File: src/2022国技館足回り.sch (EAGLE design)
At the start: 12 parts

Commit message: 国技館足回り回路の追加
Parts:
- removed MAT_LED: 02-JST, con-jst-xh:02-JST
- added C1: 100nF, rcl:C-EU025-024X044
- added LED1, LED2, LED3, LED4, LED5, LED6: (no value), led:LED5MM
- added POW: 02-JST, con-jst-xh:02-JST
- added R1, R2, R3, R4, R5, R6: 100, rcl:R-EU_0204/7
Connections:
- new net BUSY: JP1.38, JP8.1
- new net LED1: JP2.22, R2.1
- new net LED2: JP2.24, R3.1
- new net LED3: JP2.26, R4.1
- new net LED4: JP2.28, R5.1
- new net LED5: JP2.30, R6.1
- new net N$1: LED3.A, R3.2
- new net N$2: LED2.A, R2.2
- new net N$3: LED1.A, R1.2
- new net N$5: LED6.A, R6.2
- new net N$6: LED5.A, R5.2
- new net N$7: LED4.A, R4.2
- new net RESET: JP1.32, JP8.8
- new net SLEEP: JP1.30, JP9.2
- new net STATUS: JP1.34, JP8.6
- new net VIN: C1.1, JP1.24, POW.2, R1.1
- new net XMIT: JP1.36, JP8.2
- net 3V3: now also JP1.16, JP8.7
- net 5V: now also JP1.18
- net ENC1_A: now also JP1.15
- net ENC1_B: now also JP1.13
- net ENC2_A: now also JP1.27
- net ENC2_B: now also JP1.25
- net ENC3_A: now also JP1.31
- net ENC3_B: now also JP1.29
- net ENC4_A: now also JP1.37
- net ENC4_B: now also JP1.35
- net GND: now also C1.2, JP1.20, JP9.8, LED1.C, LED2.C, LED3.C, LED4.C, LED5.C, LED6.C, POW.1
- net RX1: now also JP1.21, JP8.4; no longer MAT_LED.1
- net SCL: now also JP2.3
- net SDA: now also JP2.5
- net TX1: now also JP1.17, JP9.3; no longer MAT_LED.2
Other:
- note added: "IM920sL"
- note added: "LED"
- note added: "NUCLEO-F411RE"
- note added: "POW"
- moved on the sheet: JP1, JP2, JP8, JP9, SUSPENSION

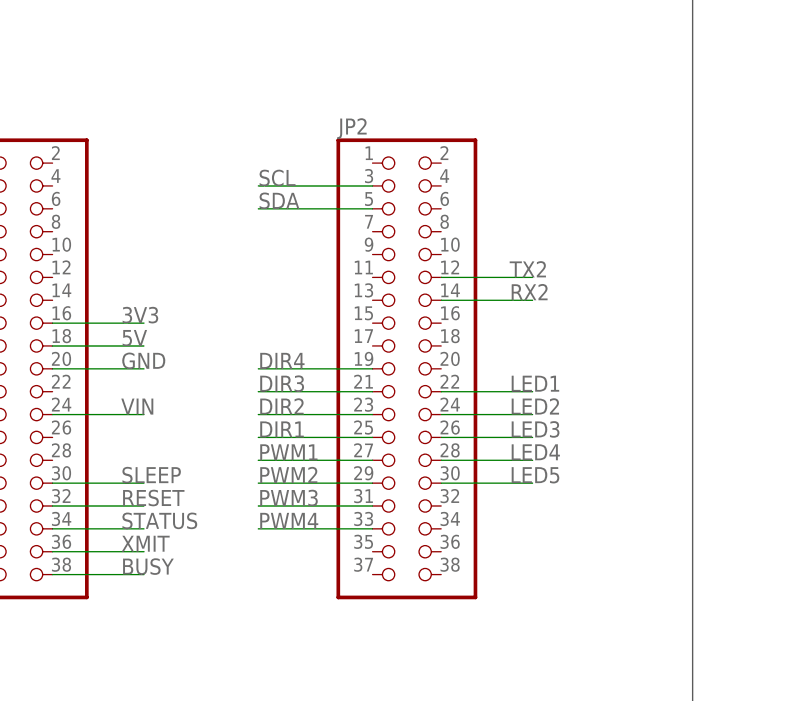
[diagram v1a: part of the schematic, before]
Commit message: 足回りコントローラ
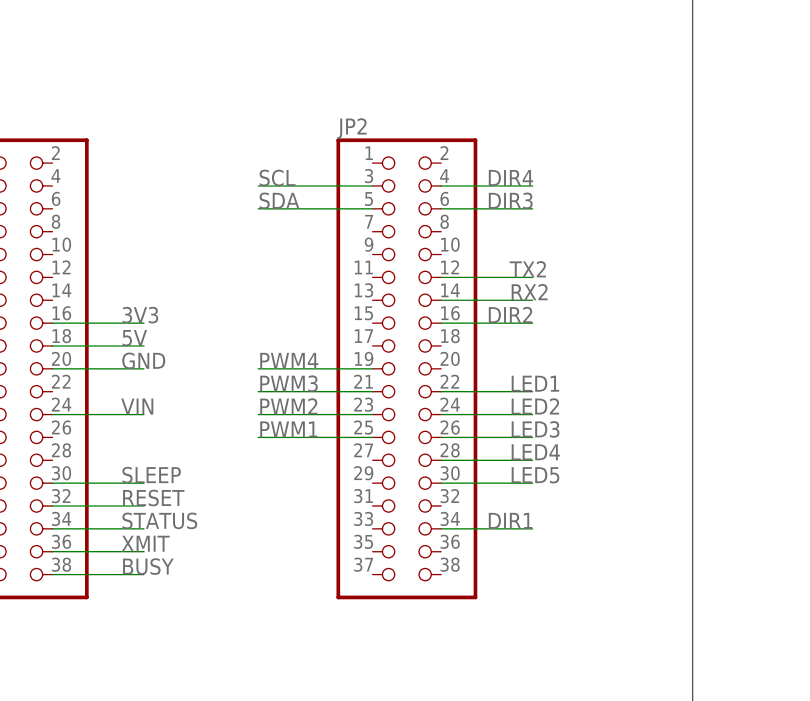
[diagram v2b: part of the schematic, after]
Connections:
- net DIR1: now also JP2.34; no longer JP2.25
- net DIR2: now also JP2.16; no longer JP2.23
- net DIR3: now also JP2.6; no longer JP2.21
- net DIR4: now also JP2.4; no longer JP2.19
- net PWM1: now also JP2.25; no longer JP2.27
- net PWM2: now also JP2.23; no longer JP2.29
- net PWM3: now also JP2.21; no longer JP2.31
- net PWM4: now also JP2.19; no longer JP2.33
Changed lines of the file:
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@@
 </segment>
 <segment>
-<pinref part="JP2" gate="G$1" pin="33"/>
-<wire x1="139.7" y1="96.52" x2="127" y2="96.52" width="0.1524" layer="91"/>
-<label x="127" y="96.52" size="1.778" layer="95"/>
+<pinref part="JP2" gate="G$1" pin="19"/>
+<wire x1="139.7" y1="114.3" x2="127" y2="114.3" width="0.1524" layer="91"/>
+<label x="127" y="114.3" size="1.778" layer="95"/>
 </segment>
 </net>
@@
 </segment>
 <segment>
-<pinref part="JP2" gate="G$1" pin="31"/>
-<wire x1="139.7" y1="99.06" x2="127" y2="99.06" width="0.1524" layer="91"/>
-<label x="127" y="99.06" size="1.778" layer="95"/>
+<pinref part="JP2" gate="G$1" pin="21"/>
+<wire x1="139.7" y1="111.76" x2="127" y2="111.76" width="0.1524" layer="91"/>
+<label x="127" y="111.76" size="1.778" layer="95"/>
 </segment>
 </net>
@@
 </segment>
 <segment>
-<pinref part="JP2" gate="G$1" pin="29"/>
-<wire x1="139.7" y1="101.6" x2="127" y2="101.6" width="0.1524" layer="91"/>
-<label x="127" y="101.6" size="1.778" layer="95"/>
+<pinref part="JP2" gate="G$1" pin="23"/>
+<wire x1="139.7" y1="109.22" x2="127" y2="109.22" width="0.1524" layer="91"/>
+<label x="127" y="109.22" size="1.778" layer="95"/>
 </segment>
 </net>
@@
 </segment>
 <segment>
-<pinref part="JP2" gate="G$1" pin="27"/>
-<wire x1="139.7" y1="104.14" x2="127" y2="104.14" width="0.1524" layer="91"/>
-<label x="127" y="104.14" size="1.778" layer="95"/>
+<pinref part="JP2" gate="G$1" pin="25"/>
+<wire x1="139.7" y1="106.68" x2="127" y2="106.68" width="0.1524" layer="91"/>
+<label x="127" y="106.68" size="1.778" layer="95"/>
 </segment>
 </net>
@@
 </segment>
 <segment>
-<pinref part="JP2" gate="G$1" pin="19"/>
-<wire x1="139.7" y1="114.3" x2="127" y2="114.3" width="0.1524" layer="91"/>
-<label x="127" y="114.3" size="1.778" layer="95"/>
+<pinref part="JP2" gate="G$1" pin="4"/>
+<wire x1="147.32" y1="134.62" x2="157.48" y2="134.62" width="0.1524" layer="91"/>
+<label x="152.4" y="134.62" size="1.778" layer="95"/>
 </segment>
 </net>
@@
 </segment>
 <segment>
-<pinref part="JP2" gate="G$1" pin="21"/>
-<wire x1="139.7" y1="111.76" x2="127" y2="111.76" width="0.1524" layer="91"/>
-<label x="127" y="111.76" size="1.778" layer="95"/>
+<pinref part="JP2" gate="G$1" pin="6"/>
+<wire x1="147.32" y1="132.08" x2="157.48" y2="132.08" width="0.1524" layer="91"/>
+<label x="152.4" y="132.08" size="1.778" layer="95"/>
 </segment>
 </net>
@@
 </segment>
 <segment>
-<pinref part="JP2" gate="G$1" pin="23"/>
-<wire x1="139.7" y1="109.22" x2="127" y2="109.22" width="0.1524" layer="91"/>
-<label x="127" y="109.22" size="1.778" layer="95"/>
+<pinref part="JP2" gate="G$1" pin="16"/>
+<wire x1="147.32" y1="119.38" x2="157.48" y2="119.38" width="0.1524" layer="91"/>
+<label x="152.4" y="119.38" size="1.778" layer="95"/>
 </segment>
 </net>
@@
 </segment>
 <segment>
-<pinref part="JP2" gate="G$1" pin="25"/>
-<wire x1="139.7" y1="106.68" x2="127" y2="106.68" width="0.1524" layer="91"/>
-<label x="127" y="106.68" size="1.778" layer="95"/>
+<pinref part="JP2" gate="G$1" pin="34"/>
+<wire x1="147.32" y1="96.52" x2="157.48" y2="96.52" width="0.1524" layer="91"/>
+<label x="152.4" y="96.52" size="1.778" layer="95"/>
 </segment>
 </net>

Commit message: 国技館足回り修正前
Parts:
- removed JP7: (no value), pinhead:PINHD-1X4
- added REMOTE_SW: 02-JST, con-jst-xh:02-JST
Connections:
- removed net SCL: JP2.3, JP7.1
- removed net SDA: JP2.5, JP7.2
- new net EMERGENCY: JP2.2, REMOTE_SW.2
- net 3V3: no longer JP7.3
- net ENC2_A: now also JP1.1; no longer JP1.27
- net ENC2_B: now also JP1.3; no longer JP1.25
- net ENC3_A: now also JP2.5; no longer JP1.31
- net ENC3_B: now also JP2.3; no longer JP1.29
- net GND: now also REMOTE_SW.1; no longer JP7.4
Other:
- note added: "EMERGENCY"
- note removed: "LSM9DS1"
- moved on the sheet: C1, POW, SUSPENSION

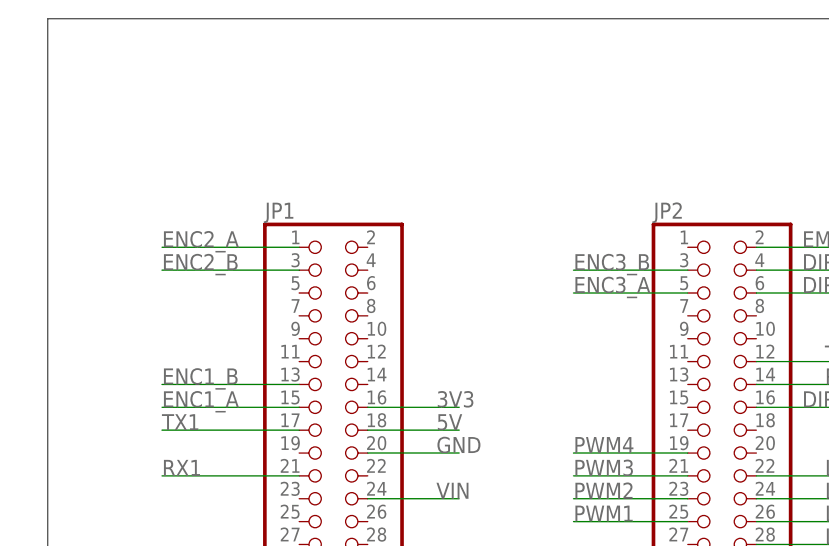
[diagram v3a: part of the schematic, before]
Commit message: 国技館足回り修正後
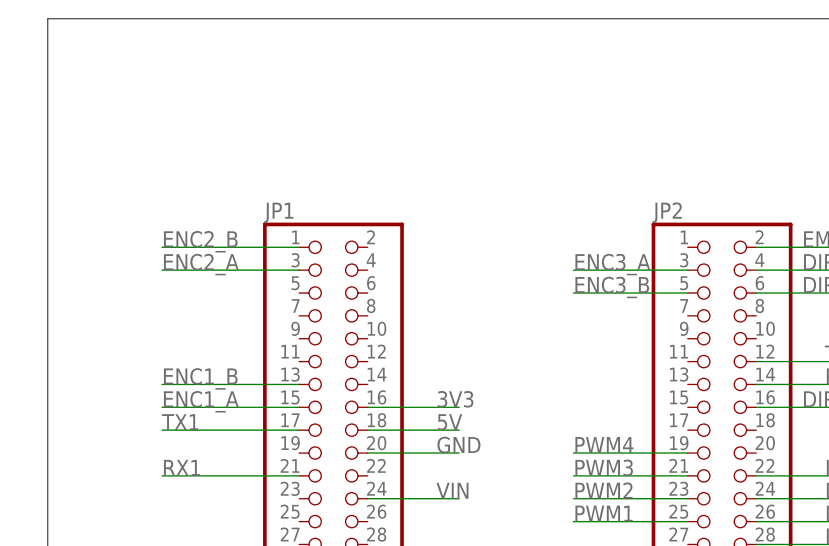
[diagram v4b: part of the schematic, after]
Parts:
- R2, R3, R4, R5, R6: device rcl:R-EU_0204/7 -> rcl:R-EU_0207/2V
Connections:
- net ENC2_A: now also JP1.3; no longer JP1.1
- net ENC2_B: now also JP1.1; no longer JP1.3
- net ENC3_A: now also JP2.3; no longer JP2.5
- net ENC3_B: now also JP2.5; no longer JP2.3
